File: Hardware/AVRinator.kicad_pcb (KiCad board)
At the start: 4 copper layers, 16.5 x 33.6 mm, 46 parts, among them J2 ICSP, J3 VCOM, J4 USB_C_Receptacle_USB2.0_16P, SW1 BOOT0, U1 STM32G431K8Ux, U2 STM32G431K8Tx, U3 AP2112K-3.3, U4 AP2112K-3.3, U5 USBLC6-2SC6, U6 TXS0108EPW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

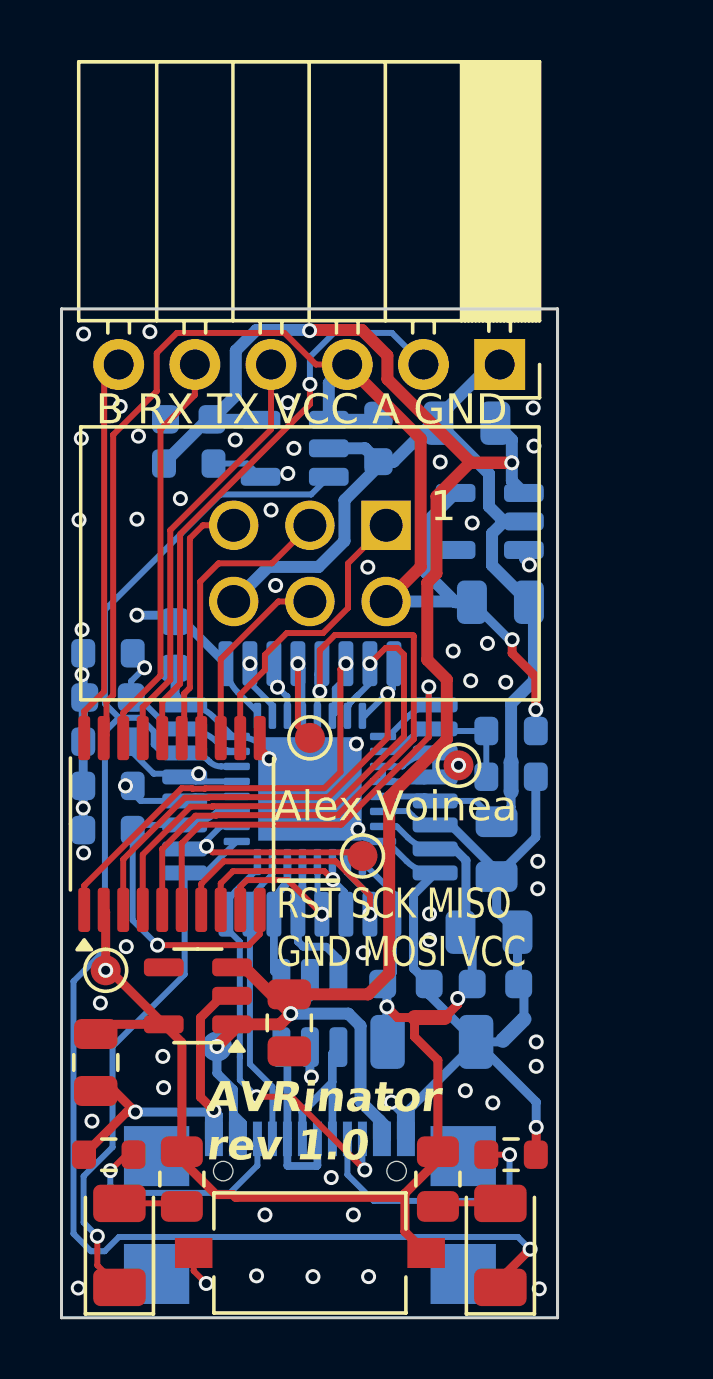
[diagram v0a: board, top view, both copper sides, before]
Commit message: Add TXS0108EPW decoupling cap and tune skew of usb
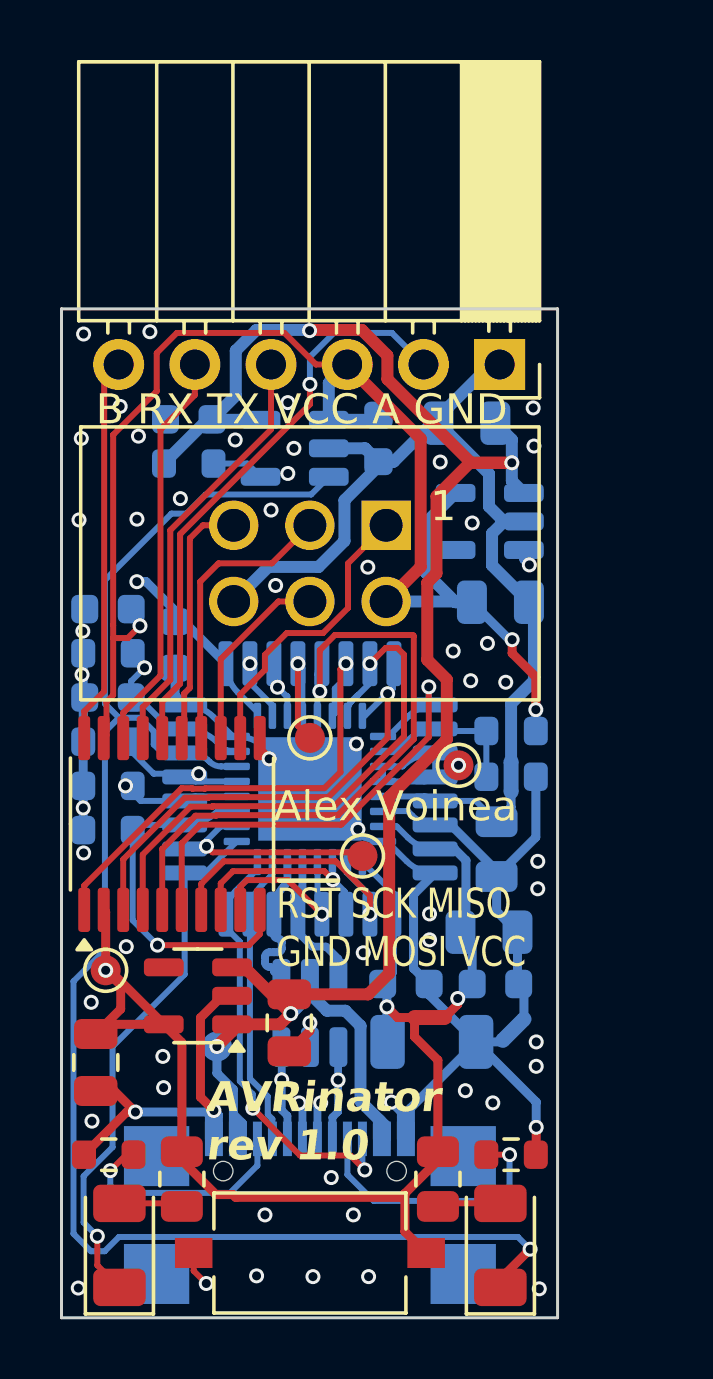
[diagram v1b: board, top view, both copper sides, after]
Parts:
- added C12: 100nF, Capacitor_SMD:C_0603_1608Metric, B.Cu at (55.5, 58.9)
- moved SYM1 15.8 mm to (55.8, 71.5)
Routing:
- net +3.3V: track 54.6 -> 59.1 mm
- net T_VCC: track 46.9 -> 48.7 mm, vias 2 -> 3
- net GND: track 51.8 -> 52.8 mm
- net /USB_D+: track 4.12 -> 4.84 mm
- net /NFAULT: track 53.3 -> 53.9 mm
- net VBUS: track 65.1 -> 65.6 mm
- net /CONN_D-: track 6.41 -> 6.06 mm, vias 0 -> 2
- net /CONN_D+: track 5.93 -> 6.06 mm, vias 0 -> 2
